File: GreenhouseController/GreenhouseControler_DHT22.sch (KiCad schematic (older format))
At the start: 3 parts

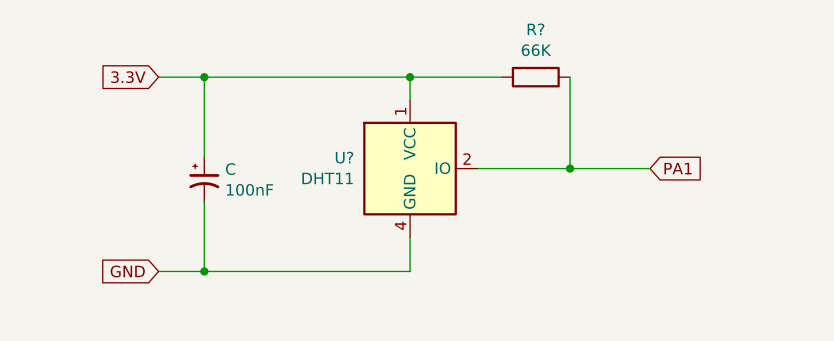
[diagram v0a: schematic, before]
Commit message: Update GreenhouseControler_DHT22.sch
Changed the Labels
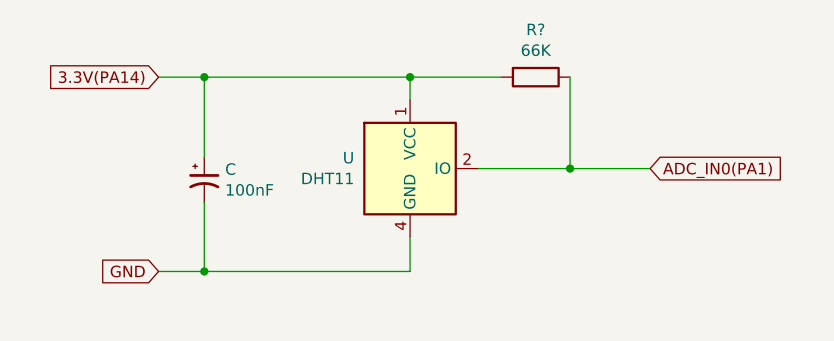
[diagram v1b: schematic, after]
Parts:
- gave numbers to parts that had none: 1
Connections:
- net 3.3V renamed 3.3V(PA14)
- net PA1 renamed ADC_IN0(PA1)
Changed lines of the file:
@@
 $EndDescr
 $Comp
-L Sensor:DHT11 U?
+L Sensor:DHT11 U
 U 1 1 619945DD
 P 5100 2750
-F 0 "U?" H 4856 2796 50  0000 R CNN
+F 0 "U" H 4856 2796 50  0000 R CNN
 F 1 "DHT11" H 4856 2705 50  0000 R CNN
 F 2 "Sensor:Aosong_DHT11_5.5x12.0_P2.54mm" H 5100 2350 50  0001 C CNN
@@
 	1    0    0    -1
 $EndComp
-Text GLabel 4000 2350 0    50   Input ~ 0
-3.3V
 Text GLabel 6150 2750 2    50   Input ~ 0
-PA1
+ADC_IN0(PA1)
 Text GLabel 4000 3200 0    50   Input ~ 0
 GND
@@
 Wire Wire Line
 	5800 2750 6150 2750
+Text GLabel 4000 2350 0    50   Input ~ 0
+3.3V(PA14)
 $EndSCHEMATC

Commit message: Connect my schematic to stm32 board
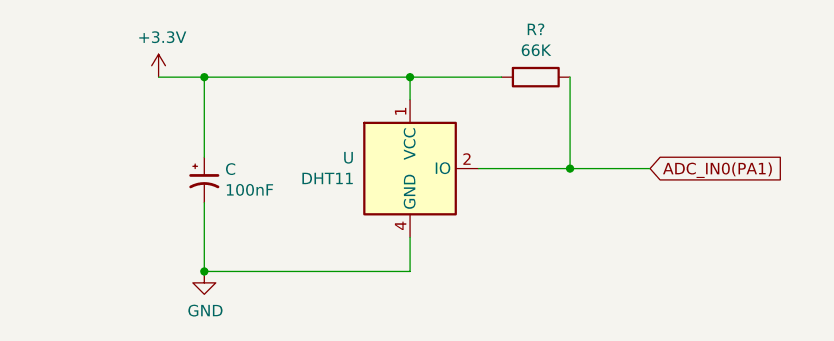
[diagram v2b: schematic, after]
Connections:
- net 3.3V(PA14) renamed +3V3
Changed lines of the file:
@@
 Text GLabel 6150 2750 2    50   Input ~ 0
 ADC_IN0(PA1)
-Text GLabel 4000 3200 0    50   Input ~ 0
-GND
 Wire Wire Line
 	4000 2350 4200 2350
 Wire Wire Line
 	5100 2350 5100 2450
-Wire Wire Line
-	4000 3200 4200 3200
 Wire Wire Line
 	5100 3200 5100 3050
@@
 Wire Wire Line
 	4200 2900 4200 3200
-Connection ~ 4200 3200
 Wire Wire Line
 	4200 3200 5100 3200
@@
 Wire Wire Line
 	5800 2750 6150 2750
-Text GLabel 4000 2350 0    50   Input ~ 0
-3.3V(PA14)
+$Comp
+L power:GND #PWR?
+U 1 1 6199D502
+P 4200 3200
+F 0 "#PWR?" H 4200 2950 50  0001 C CNN
+F 1 "GND" H 4205 3027 50  0000 C CNN
+F 2 "" H 4200 3200 50  0001 C CNN
+F 3 "" H 4200 3200 50  0001 C CNN
+	1    4200 3200
+	1    0    0    -1
+$EndComp
+Connection ~ 4200 3200
+$Comp
+L power:+3.3V #PWR?
+U 1 1 6199E09B
+P 4000 2350
+F 0 "#PWR?" H 4000 2200 50  0001 C CNN
+F 1 "+3.3V" H 4015 2523 50  0000 C CNN
+F 2 "" H 4000 2350 50  0001 C CNN
+F 3 "" H 4000 2350 50  0001 C CNN
+	1    4000 2350
+	1    0    0    -1
+$EndComp
 $EndSCHEMATC
